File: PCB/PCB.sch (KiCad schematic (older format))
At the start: 52 parts, among them J1 Conn_01x03, J2 Conn_01x02, Q1 2N2907, Q10 TIP32, Q11 BD138, Q12 TIP31, Q13 2N2222, Q2 2N2907, Q3 2N2907, Q4 2N2222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

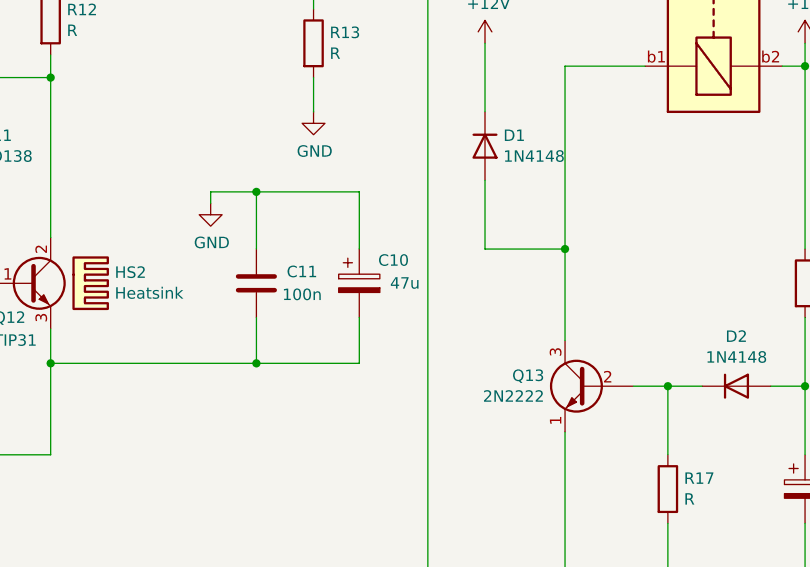
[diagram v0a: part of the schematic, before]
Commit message: C10 corrigé
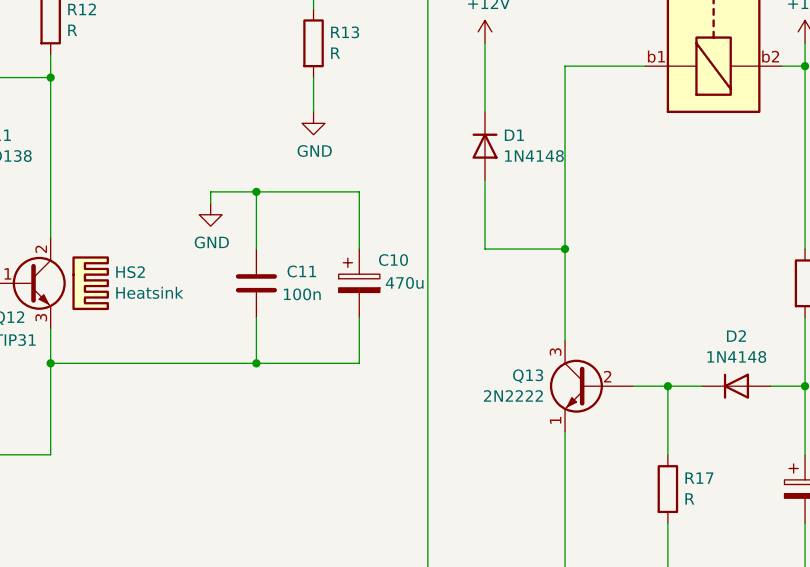
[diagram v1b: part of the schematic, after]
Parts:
- C10: value 47u -> 470u; footprint CmpAmpliAudio:CP_Radial_D8.0mm_P5.00mm -> CmpAmpliAudio:CP_Radial_D12.5mm_P5.00mm

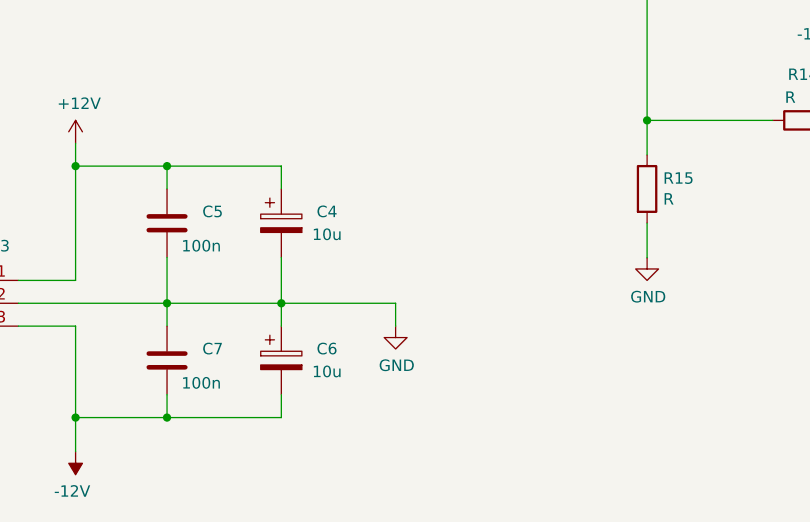
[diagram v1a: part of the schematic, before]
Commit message: 1er routage pas top
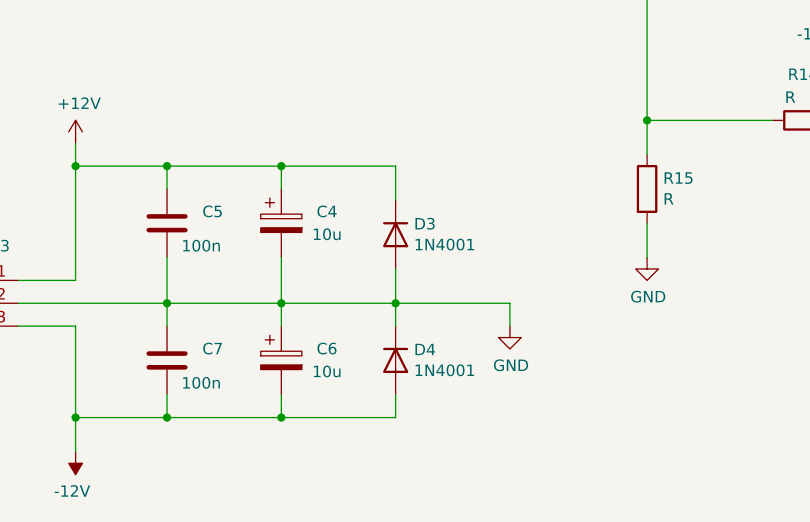
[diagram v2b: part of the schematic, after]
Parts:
- added D3, D4: 1N4001, Diode_THT:D_DO-41_SOD81_P10.16mm_Horizontal, symbol Diode:1N4001
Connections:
- net +12V: now also D3.1 (K)
- net -12V: now also D4.2 (A)
- net GND: now also D3.2 (A), D4.1 (K)
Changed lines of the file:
@@
 L power:GND #PWR017
 U 1 1 605D602F
-P 2850 6700
-F 0 "#PWR017" H 2850 6450 50  0001 C CNN
-F 1 "GND" H 2855 6527 50  0000 C CNN
-F 2 "" H 2850 6700 50  0001 C CNN
-F 3 "" H 2850 6700 50  0001 C CNN
-	1    2850 6700
+P 3350 6700
+F 0 "#PWR017" H 3350 6450 50  0001 C CNN
+F 1 "GND" H 3355 6527 50  0000 C CNN
+F 2 "" H 3350 6700 50  0001 C CNN
+F 3 "" H 3350 6700 50  0001 C CNN
+	1    3350 6700
 	1    0    0    -1
 $EndComp
@@
 	1200 6600 1850 6600
 Wire Wire Line
-	2850 6600 2850 6700
+	3350 6600 3350 6700
 Wire Wire Line
 	4500 5800 3950 5800
@@
 Connection ~ 2350 6600
 Wire Wire Line
-	2350 6600 2850 6600
+	2850 6600 3350 6600
 Wire Wire Line
 	2350 6600 2350 6700
@@
 	1    0    0    -1
 $EndComp
+$Comp
+L Diode:1N4001 D3
+U 1 1 60736985
+P 2850 6300
+F 0 "D3" V 2804 6380 50  0000 L CNN
+F 1 "1N4001" V 2895 6380 50  0000 L CNN
+F 2 "Diode_THT:D_DO-41_SOD81_P10.16mm_Horizontal" H 2850 6125 50  0001 C CNN
+F 3 "http://www.vishay.com/docs/88503/1n4001.pdf" H 2850 6300 50  0001 C CNN
+	1    2850 6300
+	0    1    1    0
+$EndComp
+$Comp
+L Diode:1N4001 D4
+U 1 1 60740ACB
+P 2850 6850
+F 0 "D4" V 2804 6930 50  0000 L CNN
+F 1 "1N4001" V 2895 6930 50  0000 L CNN
+F 2 "Diode_THT:D_DO-41_SOD81_P10.16mm_Horizontal" H 2850 6675 50  0001 C CNN
+F 3 "http://www.vishay.com/docs/88503/1n4001.pdf" H 2850 6850 50  0001 C CNN
+	1    2850 6850
+	0    1    1    0
+$EndComp
+Wire Wire Line
+	2350 6000 2850 6000
+Wire Wire Line
+	2850 6000 2850 6150
+Connection ~ 2350 6000
+Wire Wire Line
+	2850 6450 2850 6600
+Wire Wire Line
+	2850 6600 2350 6600
+Connection ~ 2850 6600
+Wire Wire Line
+	2850 6600 2850 6700
+Wire Wire Line
+	2850 7000 2850 7100
+Wire Wire Line
+	2850 7100 2350 7100
+Connection ~ 2350 7100
 $EndSCHEMATC
